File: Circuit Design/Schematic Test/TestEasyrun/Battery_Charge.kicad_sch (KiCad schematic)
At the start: 10 parts

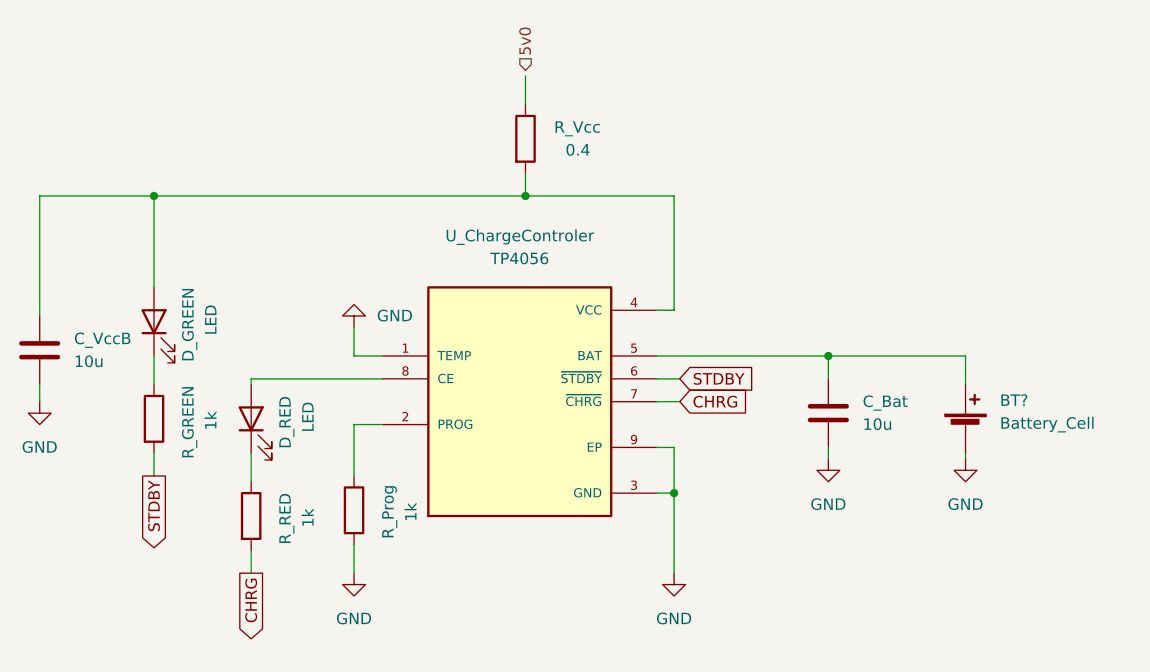
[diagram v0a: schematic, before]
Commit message: Change the global labels
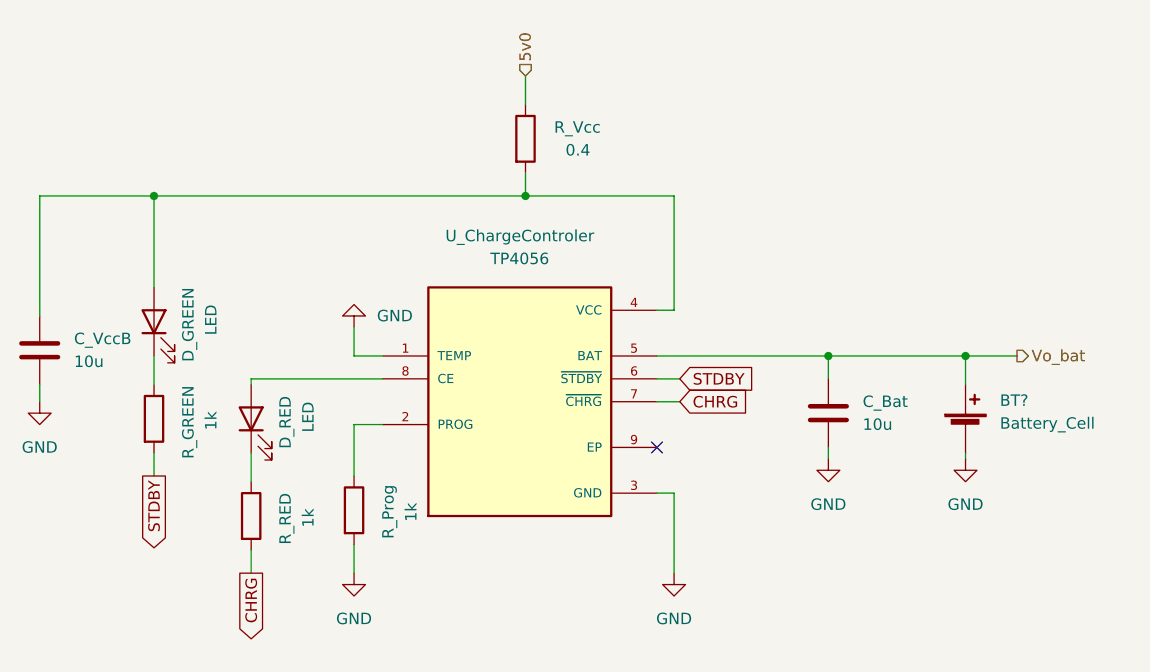
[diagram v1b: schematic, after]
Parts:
- D_GREEN, D_RED: footprint (none) -> LED_SMD:LED_0805_2012Metric_Pad1.15x1.40mm_HandSolder
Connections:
- net 5v0: now also R_Vcc.1
- net GND: no longer U_ChargeControler.9 (EP)
- net Vo_bat: now reaches BT?.1 (+), C_Bat.1, U_ChargeControler.5 (BAT)
- no-connect marks 0 -> 1
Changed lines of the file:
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@@
 (kicad_sch (version 20211123) (generator eeschema)
   (paper "A4")
+  (junction (at 196.215 97.155) (diameter 0) (color 0 0 0 0)
+  )
   (junction (at 106.045 79.375) (diameter 0) (color 0 0 0 0)
   )
@@
   (junction (at 147.32 79.375) (diameter 0) (color 0 0 0 0)
   )
-  (junction (at 163.83 112.395) (diameter 0) (color 0 0 0 0)
-  )
+  (no_connect (at 161.925 107.315))
   (wire (pts (xy 180.975 97.155) (xy 180.975 99.695))
     (stroke (width 0) (type default) (color 0 0 0 0))
@@
     (stroke (width 0) (type default) (color 0 0 0 0))
   )
+  (wire (pts (xy 196.215 97.155) (xy 201.93 97.155))
+    (stroke (width 0) (type default) (color 0 0 0 0))
+  )
   (wire (pts (xy 180.975 97.155) (xy 196.215 97.155))
     (stroke (width 0) (type default) (color 0 0 0 0))
@@
     (stroke (width 0) (type default) (color 0 0 0 0))
   )
-  (wire (pts (xy 163.83 107.315) (xy 163.83 112.395))
-    (stroke (width 0) (type default) (color 0 0 0 0))
-  )
   (wire (pts (xy 116.84 99.695) (xy 116.84 100.33))
     (stroke (width 0) (type default) (color 0 0 0 0))
@@
   )
   (wire (pts (xy 147.32 66.04) (xy 147.32 69.215))
-    (stroke (width 0) (type default) (color 0 0 0 0))
-  )
-  (wire (pts (xy 161.925 107.315) (xy 163.83 107.315))
     (stroke (width 0) (type default) (color 0 0 0 0))
   )
@@
     )
   )
-  (hierarchical_label "5v0" (shape input) (at 147.32 65.405 90)
+  (hierarchical_label "Vo_bat" (shape output) (at 201.93 97.155 0)
+    (effects (font (size 1.27 1.27)) (justify left))
+  )
+  (hierarchical_label "5v0" (shape input) (at 147.32 66.04 90)
     (effects (font (size 1.27 1.27)) (justify left))
   )
@@
       (effects (font (size 1.27 1.27)) (justify right))
     )
-    (property "Footprint" "" (id 2) (at 116.84 104.14 0)
+    (property "Footprint" "LED_SMD:LED_0805_2012Metric_Pad1.15x1.40mm_HandSolder" (id 2) (at 116.84 104.14 0)
       (effects (font (size 1.27 1.27)) hide)
     )
@@
       (effects (font (size 1.27 1.27)) (justify right))
     )
-    (property "Footprint" "" (id 2) (at 106.045 93.345 0)
-      (effects (font (size 1.27 1.27)) hide)
-    )
+    (property "Footprint" "LED_SMD:LED_0805_2012Metric_Pad1.15x1.40mm_HandSolder" (id 2) (at 106.045 93.345 0)
+      (effects (font (size 1.27 1.27)) hide)
+    )
